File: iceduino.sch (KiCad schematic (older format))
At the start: 0 parts

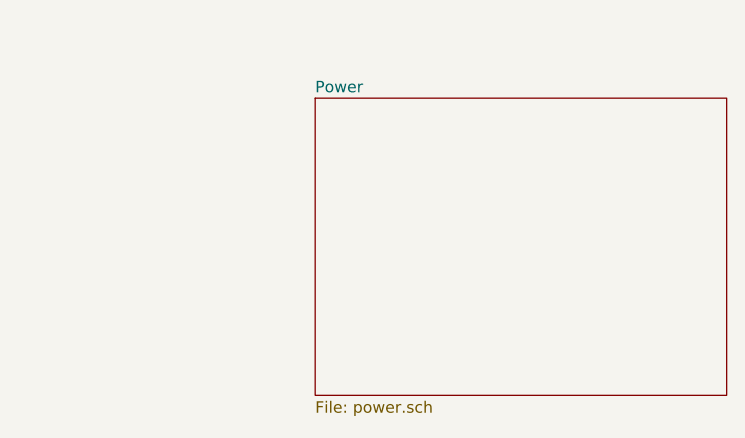
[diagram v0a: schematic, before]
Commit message: 7-17VIN Power
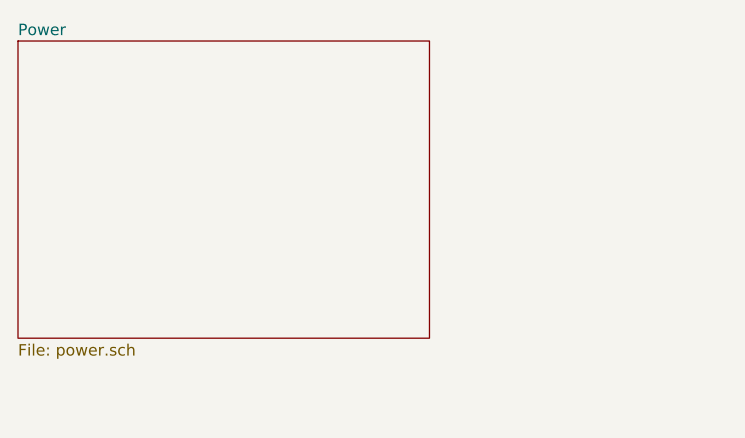
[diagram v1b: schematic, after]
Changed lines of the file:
@@
 $EndDescr
 $Sheet
-S 3250 2050 1800 1300
+S 1950 1800 1800 1300
 U 5ECD2614
 F0 "Power" 50

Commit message: ui sheet
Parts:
- added U?: ICE40HX4K-TQ144, symbol ice40hx4k:ICE40HX4K-TQ144
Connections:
- new net ADC_SCL_3V3: U?.120 (IOT_179)
- new net ADC_SDA_3V3: U?.121 (IOT_181)
- new net LED0: U?.112 (IOT_169)
- new net LED1: U?.113 (IOT_170)
- new net LED2: U?.114 (IOT_171)
- new net LED3: U?.115 (IOT_172)
- new net LED4: U?.116 (IOT_173)
- new net LED5: U?.117 (IOT_174)
- new net LED6: U?.118 (IOT_177)
- new net LED7: U?.119 (IOT_178)
- new net P10_1: U?.137 (IOT_215)
- new net P1_1: U?.143 (IOT_221)
- new net P2_1: U?.141 (IOT_219)
- new net P3_1: U?.138 (IOT_216)
- new net P4_1: U?.136 (IOT_214)
- new net P7_1: U?.144 (IOT_222)
- new net P8_1: U?.142 (IOT_220)
- new net P9_1: U?.139 (IOT_217)
- new net SW1: U?.122 (IOT_190)
- new net SW2: U?.124 (IOT_191)
- new net SW3: U?.125 (IOT_192)
- new net SW4: U?.128 (IOT_197_GBIN1)
- new net SW5: U?.129 (IOT_198_GBIN0)
- new net SW6: U?.130 (IOT_206)
- new net SW7: U?.134 (IOT_212)
- new net ~SRAM_CE~: U?.110 (IOT_168)
- no-connect marks 0 -> 1
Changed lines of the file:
@@
 $Descr A4 11693 8268
 encoding utf-8
-Sheet 1 6
+Sheet 1 7
 Title ""
 Date ""
@@
 F1 "power.sch" 50
 $EndSheet
+$Sheet
+S 5250 2350 1950 1200
+U 5F70B37B
+F0 "USER_INTERFACE" 50
+F1 "ui.sch" 50
+F2 "LED[0..7]" I L 5250 2950 50
+F3 "SW[1..7]" O R 7200 2950 50
+$EndSheet
+Wire Wire Line
+	8700 3000 8950 3000
+Text Label 8700 3000 0    50   ~ 0
+SW7
+Wire Wire Line
+	8700 2900 8950 2900
+Text Label 8700 2900 0    50   ~ 0
+SW6
+Wire Wire Line
+	8675 1300 8950 1300
+Text GLabel 8675 1300 0    39   Output ~ 0
+~SRAM_CE~
+Wire Wire Line
+	8700 2800 8950 2800
+Text Label 8700 2800 0    50   ~ 0
+SW5
+Wire Wire Line
+	8700 2700 8950 2700
+Text Label 8700 2700 0    50   ~ 0
+SW4
+Wire Wire Line
+	8700 2600 8950 2600
+Text Label 8700 2600 0    50   ~ 0
+SW3
+Wire Wire Line
+	8700 2500 8950 2500
+Text Label 8700 2500 0    50   ~ 0
+SW2
+Wire Wire Line
+	8700 2400 8950 2400
+Text Label 8700 2400 0    50   ~ 0
+SW1
+Wire Wire Line
+	8700 2100 8950 2100
+Text Label 8700 2100 0    50   ~ 0
+LED7
+Wire Wire Line
+	8700 2000 8950 2000
+Text Label 8700 2000 0    50   ~ 0
+LED6
+Wire Wire Line
+	8700 1900 8950 1900
+Text Label 8700 1900 0    50   ~ 0
+LED5
+Wire Wire Line
+	8700 1800 8950 1800
+Text Label 8700 1800 0    50   ~ 0
+LED4
+Wire Wire Line
+	8700 1700 8950 1700
+Text Label 8700 1700 0    50   ~ 0
+LED3
+Wire Wire Line
+	8700 1600 8950 1600
+Text Label 8700 1600 0    50   ~ 0
+LED2
+Wire Wire Line
+	8700 1500 8950 1500
+Text Label 8700 1500 0    50   ~ 0
+LED1
+Wire Wire Line
+	8700 1400 8950 1400
+Text Label 8700 1400 0    50   ~ 0
+LED0
+$Comp
+L ice40hx4k:ICE40HX4K-TQ144 U?
+U 2 1 5F791B82
+P 9150 2600
+AR Path="/5F791B82" Ref="U?"  Part="2"
+AR Path="/5CAB7CD4/5F791B82" Ref="U?"  Part="2"
+AR Path="/5F70B37B/5F791B82" Ref="U?"  Part="2"
+F 0 "U?" H 9150 1125 50  0000 L CNN
+F 1 "ICE40HX4K-TQ144" H 9350 4050 50  0000 L CNN
+F 2 "" H 9150 2600 50  0001 C CNN
+F 3 "" H 9150 2600 50  0001 C CNN
+F 4 "IC FPGA 107 I/O 144TQFP" H 700 -250 50  0001 C CNN "Description"
+F 5 "220-1572-ND" H 700 -250 50  0001 C CNN "Digikey"
+F 6 "Lattice Semiconductor Corporation" H 700 -250 50  0001 C CNN "Mfg Name"
+F 7 "ICE40HX4K-TQ144" H 700 -250 50  0001 C CNN "Mfg Part Num"
+F 8 "Spec" H 700 -250 50  0001 C CNN "Spec"
+	2    9150 2600
+	1    0    0    -1
+$EndComp
+NoConn ~ 8950 3100
+Wire Wire Line
+	8725 3900 8950 3900
+Wire Wire Line
+	8725 3700 8950 3700
+Wire Wire Line
+	8725 3500 8950 3500
+Wire Wire Line
+	8725 3300 8950 3300
+Wire Wire Line
+	8725 3800 8950 3800
+Wire Wire Line
+	8725 3600 8950 3600
+Wire Wire Line
+	8725 3400 8950 3400
+Wire Wire Line
+	8725 3200 8950 3200
+Text GLabel 8725 3800 0    50   BiDi ~ 0
+P1_1
+Text GLabel 8725 3600 0    50   BiDi ~ 0
+P2_1
+Text GLabel 8725 3400 0    50   BiDi ~ 0
+P3_1
+Text GLabel 8725 3200 0    50   BiDi ~ 0
+P4_1
+Text GLabel 8725 3900 0    50   BiDi ~ 0
+P7_1
+Text GLabel 8725 3700 0    50   BiDi ~ 0
+P8_1
+Text GLabel 8725 3500 0    50   BiDi ~ 0
+P9_1
+Text GLabel 8725 3300 0    50   BiDi ~ 0
+P10_1
+Text GLabel 8675 2300 0    50   BiDi ~ 0
+ADC_SDA_3V3
+Text GLabel 8675 2200 0    50   BiDi ~ 0
+ADC_SCL_3V3
+Wire Wire Line
+	8675 2200 8950 2200
+Wire Wire Line
+	8675 2300 8950 2300
+Wire Bus Line
+	7200 2950 7800 2950
+Wire Bus Line
+	5250 2950 4700 2950
+Text Label 4775 2950 0    50   ~ 0
+LED[0..7]
+Text Label 7400 2950 0    50   ~ 0
+SW[1..7]
 $EndSCHEMATC

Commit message: Schematic modified (Hierarchy) Bug where SPI was active when creset or ss was low fixed PCB layout started (almost all parts are at position) No parts on the bottom so far Arduino and PMOD header spacings corrected according to its standards
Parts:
- added D10, D9: CDBU5020, Diode_SMD:D_0603_1608Metric, symbol Device:D_ALT
- added H1, H2, H3, H4: MountingHole, MountingHole:MountingHole_3mm, symbol Mechanical:MountingHole
- added unit 1 of U1
- added unit 4 of U1
- added unit 5 of U1
- added unit 6 of U1
- added unit 7 of U1
- added unit 3 of U1
- U1: renamed from U?; footprint (none) -> Package_QFP:TQFP-144_20x20mm_P0.5mm
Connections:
- new net: D10.1 (K), U1.108 (VPP_2V5)
- new net: U1.133 (NC[7]), U1.35 (NC), U1.36 (NC), U1.50 (NC), U1.51 (NC), U1.58 (NC), U1.77 (NC)
- new net +1V2: U1.111 (VCC[4]), U1.27 (VCC), U1.40 (VCC), U1.92 (VCC)
- new net +3V3: D10.2 (A), U1.100 (VCCIO_1[2]), U1.123 (VCCIO_0), U1.131 (VCCIO_0[2]), U1.30 (VCCIO_3[2]), U1.46 (VCCIO_2), U1.57 (VCCIO_2[2]), U1.6 (VCCIO_3), U1.72 (VCC_SPI), U1.89 (VCCIO_1)
- new net A0: U1.73 (IOR_109)
- new net A1: U1.74 (IOR_110)
- new net A10: U1.101 (IOR_160)
- new net A11: U1.99 (IOR_152)
- new net A12: U1.98 (IOR_148)
- new net A13: U1.97 (IOR_147)
- new net A14: U1.96 (IOR_146)
- new net A15: U1.85 (IOR_128)
- new net A16: U1.83 (IOR_119)
- new net A17: U1.81 (IOR_117)
- new net A18: U1.79 (IOR_115)
- new net A2: U1.75 (IOR_111)
- new net A3: U1.76 (IOR_112)
- new net A4: U1.78 (IOR_114)
- new net A5: U1.102 (IOR_161)
- new net A6: U1.104 (IOR_164)
- new net A7: U1.105 (IOR_165)
- new net A8: U1.106 (IOR_166)
- new net A9: U1.107 (IOR_167)
- new net CDONE: U1.65 (CDONE)
- new net CLK_12M: U1.21 (IOL_14A_GBIN6)
- new net CRESET_B: D9.2 (A), U1.66 (CRESET_B)
- new net FPGA_INO_D2: U1.41 (IOB_63)
- new net FPGA_INO_D3: U1.42 (IOB_64)
- new net FPGA_INO_D4: U1.43 (IOB_71)
- new net FPGA_INO_D5: U1.44 (IOB_72)
- new net FPGA_INO_D6: U1.45 (IOB_73)
- new net FPGA_INO_D7: U1.47 (IOB_79)
- new net FPGA_INO_D8: U1.33 (IOL_25A)
- new net FPGA_INO_D9: U1.32 (IOL_24B)
- new net FPGA_INO_MISO: U1.25 (IOL_18A)
- new net FPGA_INO_MOSI: U1.29 (IOL_23B)
- new net FPGA_INO_RX: U1.38 (IOB_57)
- new net FPGA_INO_SCK: U1.24 (IOL_17B)
- new net FPGA_INO_SCL: U1.28 (IOL_23A)
- new net FPGA_INO_SDA: U1.26 (IOL_18B)
- new net FPGA_INO_SS: U1.31 (IOL_24A)
- new net FPGA_INO_TX: U1.37 (IOB_56)
- new net GND: U1.103 (GND), U1.13 (GND), U1.132 (GND), U1.14 (GND), U1.140 (GND[9]), U1.5 (GND), U1.59 (GND), U1.69 (GND), U1.86 (GND)
- new net GNDPLL_0: U1.53 (GNDPLL0)
- new net GNDPLL_1: U1.127 (GNDPLL1)
- new net IC_CLK_50M: U1.52 (IOB_82_GBIN4)
- new net INO_RESET: D9.1 (K)
- new net IO0: U1.80 (IOR_116)
- new net IO1: U1.82 (IOR_118)
- new net IO2: U1.84 (IOR_120)
- new net IO3: U1.91 (IOR_139)
- new net IO4: U1.95 (IOR_144)
- new net IO5: U1.93 (IOR_140_GBIN3)
- new net IO6: U1.90 (IOR_138)
- new net IO7: U1.88 (IOR_137)
- new net MISO: U1.68 (IOB_106_SDI)
- new net MOSI: U1.67 (IOB_105_SDO)
- new net OE0: U1.39 (IOB_61)
- new net OE1: U1.34 (IOL_25B)
- new net P10_2: U1.12 (IOL_8B)
- new net P10_3: U1.2 (IOL_2B)
- new net P1_2: U1.20 (IOL_13B_GBIN7)
- new net P1_3: U1.16 (IOL_10B)
- new net P2_2: U1.19 (IOL_13A)
- new net P2_3: U1.11 (IOL_8A)
- new net P3_2: U1.17 (IOL_12A)
- new net P3_3: U1.4 (IOL_3B)
- new net P4_2: U1.15 (IOL_10A)
- new net P4_3: U1.3 (IOL_3A)
- new net P7_2: U1.18 (IOL_12B)
- new net P7_3: U1.9 (IOL_5A)
- new net P8_2: U1.8 (IOL_4B)
- new net P8_3: U1.7 (IOL_4A)
- new net P9_2: U1.10 (IOL_5B)
- new net P9_3: U1.1 (IOL_2A)
- new net PMOD_PWR_EN: U1.22 (IOL_14B)
- new net RXD: U1.60 (IOB_95)
- new net SCK: U1.70 (IOB_107_SCK)
- new net SS: U1.71 (IOB_108_SS)
- new net TXD: U1.62 (IOB_102)
- new net VCCPLL_0: U1.54 (VCCPLL0)
- new net VCCPLL_1: U1.126 (VCCPLL1)
- new net ~CTS~: U1.56 (IOB_94)
- new net ~DCD~: U1.49 (IOB_81_GBIN5)
- new net ~DSR~: U1.55 (IOB_91)
- new net ~DTR~: U1.48 (IOB_80)
- new net ~RTS~: U1.61 (IOB_96)
- new net ~SRAM_OE~: U1.87 (IOR_136)
- new net ~SRAM_WE~: U1.94 (IOR_141_GBIN2)
- no-connect marks 1 -> 6
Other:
- note added: "Power for PLLs\nGND must not be connected\nto Board Ground"
- moved on the sheet: U1B

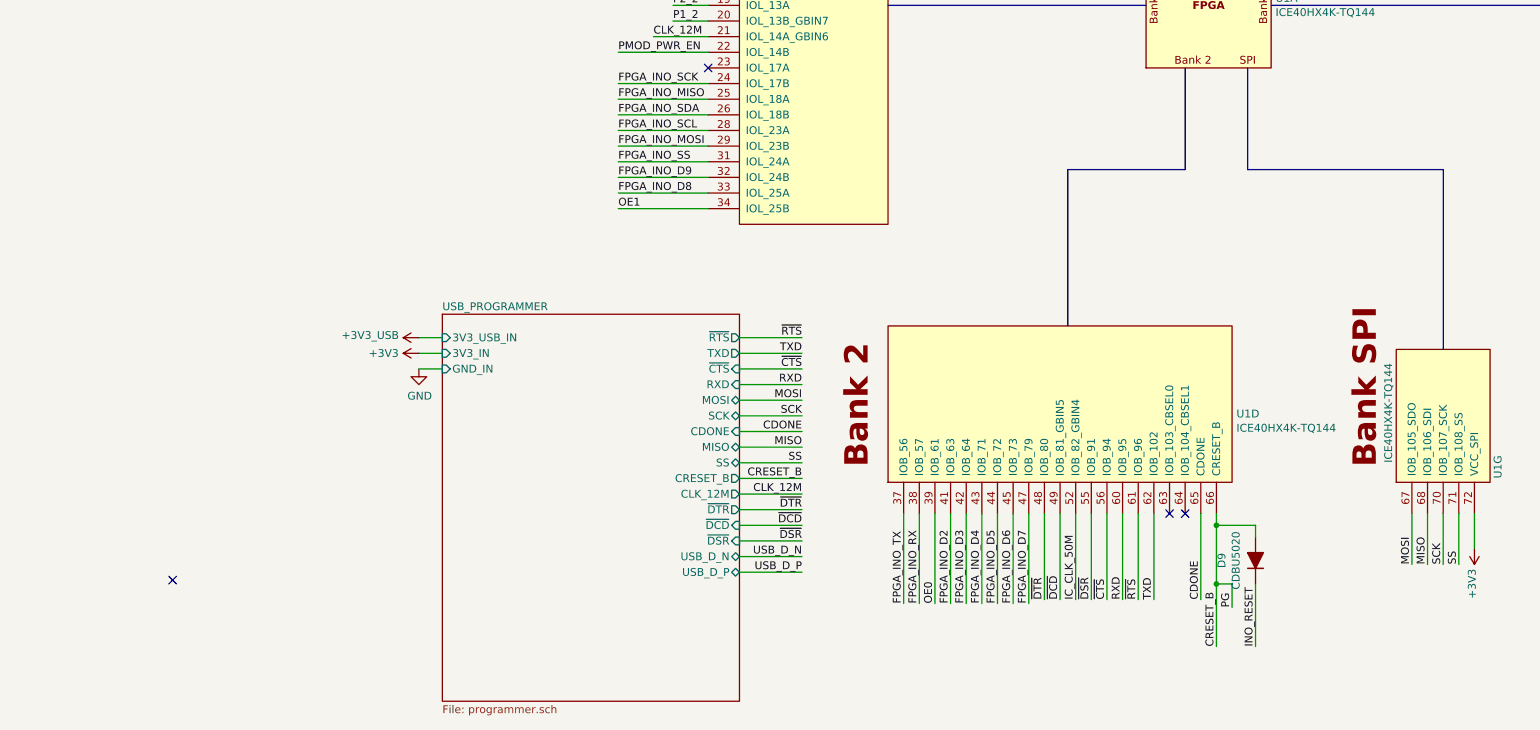
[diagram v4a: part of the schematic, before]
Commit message: Added wires for quad-SPI Flash operation
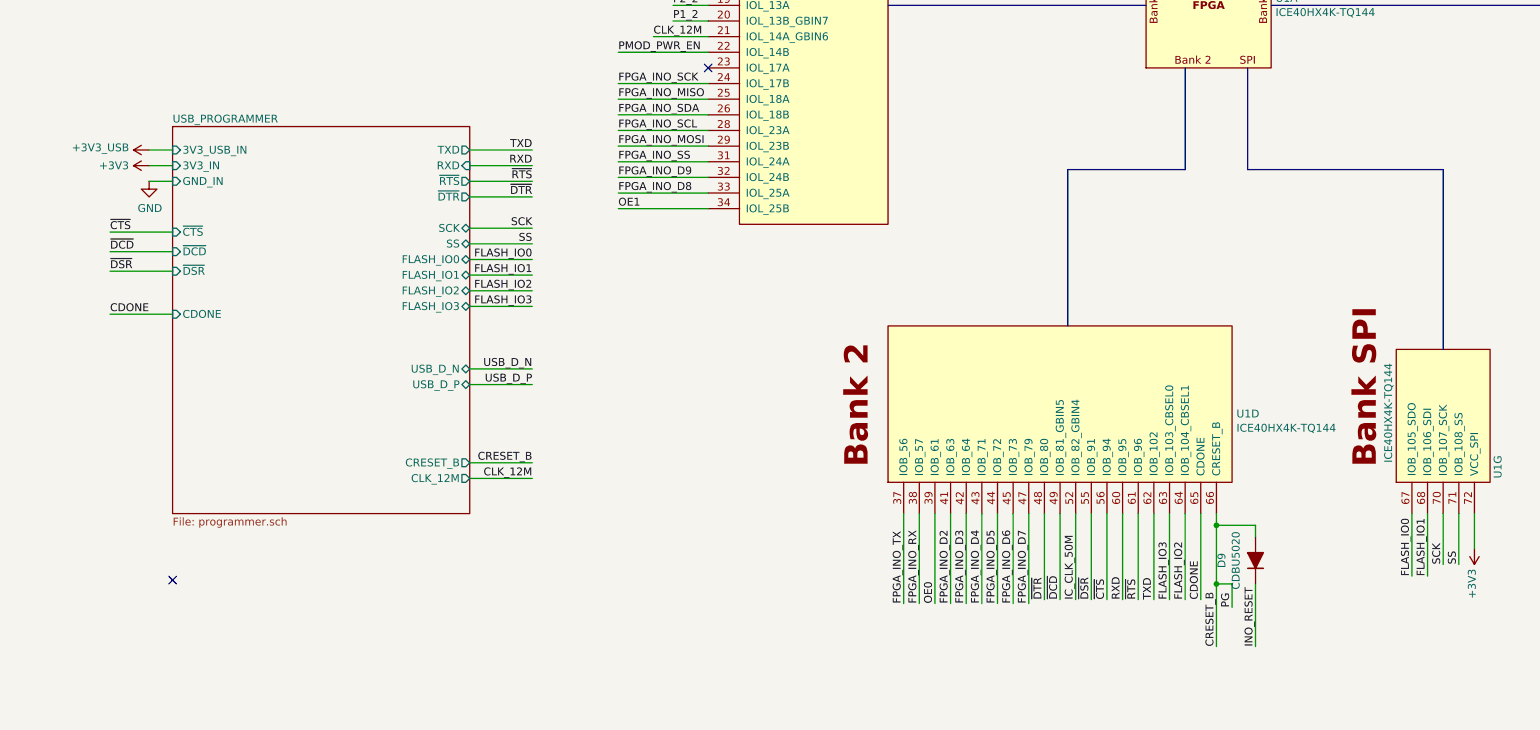
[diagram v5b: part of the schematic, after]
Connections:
- net FLASH_IO3: now reaches U1.63 (IOB_103_CBSEL0)
- net FLASH_IO2: now reaches U1.64 (IOB_104_CBSEL1)
- net MISO renamed FLASH_IO1
- net MOSI renamed FLASH_IO0
- no-connect marks 6 -> 4
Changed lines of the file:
@@
 Text Label 7350 9450 1    50   ~ 0
 IC_CLK_50M
-NoConn ~ 8050 8900
-NoConn ~ 7950 8900
 Wire Wire Line
 	8250 8900 8250 8975
@@
 	0    -1   -1   0
 $EndComp
-Text Label 9500 9225 1    50   ~ 0
-MOSI
-Wire Wire Line
-	9500 9225 9500 8900
-Text Label 9600 9225 1    50   ~ 0
-MISO
-Wire Wire Line
-	9600 9225 9600 8900
+Text Label 9500 9300 1    50   ~ 0
+FLASH_IO0
+Wire Wire Line
+	9500 9300 9500 8900
+Text Label 9600 9300 1    50   ~ 0
+FLASH_IO1
+Wire Wire Line
+	9600 9300 9600 8900
 Text Label 9700 9225 1    50   ~ 0
 SCK
@@
 Text Label 550  1250 0    50   ~ 0
 CDONE
-$Sheet
-S 3300 7625 1900 2475
-U 5ED0B946
-F0 "USB_PROGRAMMER" 50
-F1 "programmer.sch" 50
-F2 "3V3_USB_IN" I L 3300 7775 50
-F3 "3V3_IN" I L 3300 7875 50
-F4 "GND_IN" I L 3300 7975 50
-F5 "~RTS~" O R 5200 7775 50
-F6 "TXD" O R 5200 7875 50
-F7 "~CTS~" I R 5200 7975 50
-F8 "RXD" I R 5200 8075 50
-F9 "MOSI" B R 5200 8175 50
-F10 "SCK" B R 5200 8275 50
-F11 "CDONE" I R 5200 8375 50
-F12 "MISO" B R 5200 8475 50
-F13 "SS" B R 5200 8575 50
-F14 "CRESET_B" O R 5200 8675 50
-F15 "CLK_12M" O R 5200 8775 50
-F16 "~DTR~" O R 5200 8875 50
-F17 "~DCD~" I R 5200 8975 50
-F18 "~DSR~" I R 5200 9075 50
-F19 "USB_D_N" B R 5200 9175 50
-F20 "USB_D_P" B R 5200 9275 50
-$EndSheet
-Wire Wire Line
-	3300 7775 3150 7775
-Wire Wire Line
-	3300 7875 3150 7875
-Wire Wire Line
-	3300 7975 3150 7975
+Wire Wire Line
+	1575 6575 1425 6575
+Wire Wire Line
+	1575 6675 1425 6675
+Wire Wire Line
+	1575 6775 1425 6775
 $Comp
 L power_symbols:+3V3_USB #PWR01
 U 1 1 5F14A03A
-P 3150 7775
-F 0 "#PWR01" H 3150 7625 50  0001 C CNN
-F 1 "+3V3_USB" V 3165 7903 50  0000 L CNN
-F 2 "" H 3150 7775 50  0001 C CNN
-F 3 "" H 3150 7775 50  0001 C CNN
-	1    3150 7775
+P 1425 6575
+F 0 "#PWR01" H 1425 6425 50  0001 C CNN
+F 1 "+3V3_USB" V 1440 6703 50  0000 L CNN
+F 2 "" H 1425 6575 50  0001 C CNN
+F 3 "" H 1425 6575 50  0001 C CNN
+	1    1425 6575
 	0    -1   -1   0
 $EndComp
@@
 L power:GND #PWR03
 U 1 1 5F18E191
-P 3150 7975
-F 0 "#PWR03" H 3150 7725 50  0001 C CNN
-F 1 "GND" H 3155 7802 50  0000 C CNN
-F 2 "" H 3150 7975 50  0001 C CNN
-F 3 "" H 3150 7975 50  0001 C CNN
-	1    3150 7975
-	1    0    0    -1
-$EndComp
-Wire Wire Line
-	5200 7775 5600 7775
-Wire Wire Line
-	5200 7875 5600 7875
-Wire Wire Line
-	5200 7975 5600 7975
-Wire Wire Line
-	5200 8075 5600 8075
-Wire Wire Line
-	5200 8175 5600 8175
-Wire Wire Line
-	5200 8275 5600 8275
-Wire Wire Line
-	5200 8375 5600 8375
-Wire Wire Line
-	5200 8475 5600 8475
-Wire Wire Line
-	5200 8575 5600 8575
-Wire Wire Line
-	5200 8675 5600 8675
-Wire Wire Line
-	5200 8775 5600 8775
-Wire Wire Line
-	5200 8875 5600 8875
-Wire Wire Line
-	5200 8975 5600 8975
-Wire Wire Line
-	5200 9075 5600 9075
-Text Label 5600 7775 2    50   ~ 0
+P 1425 6775
+F 0 "#PWR03" H 1425 6525 50  0001 C CNN
+F 1 "GND" H 1430 6602 50  0000 C CNN
+F 2 "" H 1425 6775 50  0001 C CNN
+F 3 "" H 1425 6775 50  0001 C CNN
+	1    1425 6775
+	1    0    0    -1
+$EndComp
+Wire Wire Line
+	3475 6775 3875 6775
+Wire Wire Line
+	3475 6575 3875 6575
+Wire Wire Line
+	1575 7100 1175 7100
+Wire Wire Line
+	3475 6675 3875 6675
+Wire Wire Line
+	3475 7275 3875 7275
+Wire Wire Line
+	3475 7075 3875 7075
+Wire Wire Line
+	1575 7625 1175 7625
+Wire Wire Line
+	3475 7375 3875 7375
+Wire Wire Line
+	3475 7175 3875 7175
+Wire Wire Line
+	3475 8575 3875 8575
+Wire Wire Line
+	3475 8675 3875 8675
+Wire Wire Line
+	3475 6875 3875 6875
+Wire Wire Line
+	1575 7225 1175 7225
+Wire Wire Line
+	1575 7350 1175 7350
+Text Label 3875 6775 2    50   ~ 0
 ~RTS~
-Text Label 5600 7875 2    50   ~ 0
+Text Label 3875 6575 2    50   ~ 0
 TXD
-Text Label 5600 7975 2    50   ~ 0
+Text Label 1175 7100 0    50   ~ 0
 ~CTS~
-Text Label 5600 8075 2    50   ~ 0
+Text Label 3875 6675 2    50   ~ 0
 RXD
-Text Label 5600 8175 2    50   ~ 0
-MOSI
-Text Label 5600 8275 2    50   ~ 0
+Text Label 3875 7275 2    50   ~ 0
+FLASH_IO0
+Text Label 3875 7075 2    50   ~ 0
 SCK
-Text Label 5600 8375 2    50   ~ 0
+Text Label 1175 7625 0    50   ~ 0
 CDONE
-Text Label 5600 8475 2    50   ~ 0
-MISO
-Text Label 5600 8575 2    50   ~ 0
+Text Label 3875 7375 2    50   ~ 0
+FLASH_IO1
+Text Label 3875 7175 2    50   ~ 0
 SS
-Text Label 5600 8675 2    50   ~ 0
+Text Label 3875 8575 2    50   ~ 0
 CRESET_B
-Text Label 5600 8775 2    50   ~ 0
+Text Label 3875 8675 2    50   ~ 0
 CLK_12M
-Text Label 5600 8875 2    50   ~ 0
+Text Label 3875 6875 2    50   ~ 0
 ~DTR~
-Text Label 5600 8975 2    50   ~ 0
+Text Label 1175 7225 0    50   ~ 0
 ~DCD~
-Text Label 5600 9075 2    50   ~ 0
+Text Label 1175 7350 0    50   ~ 0
 ~DSR~
 Text Label 7150 9450 1    50   ~ 0
@@
 	4650 5850 5000 5850
 Wire Wire Line
-	5200 9175 5600 9175
-Wire Wire Line
-	5200 9275 5600 9275
-Text Label 5600 9175 2    50   ~ 0
+	3475 7975 3875 7975
+Wire Wire Line
+	3475 8075 3875 8075
+Text Label 3875 7975 2    50   ~ 0
 USB_D_N
-Text Label 5600 9275 2    50   ~ 0
+Text Label 3875 8075 2    50   ~ 0
 USB_D_P
 $Comp
@@
 L power:+3V3 #PWR0107
 U 1 1 5F527E84
-P 3150 7875
-F 0 "#PWR0107" H 3150 7725 50  0001 C CNN
-F 1 "+3V3" V 3150 8100 50  0000 C CNN
-F 2 "" H 3150 7875 50  0001 C CNN
-F 3 "" H 3150 7875 50  0001 C CNN
-	1    3150 7875
+P 1425 6675
+F 0 "#PWR0107" H 1425 6525 50  0001 C CNN
+F 1 "+3V3" V 1425 6900 50  0000 C CNN
+F 2 "" H 1425 6675 50  0001 C CNN
+F 3 "" H 1425 6675 50  0001 C CNN
+	1    1425 6675
 	0    -1   -1   0
 $EndComp
@@
 	1    0    0    -1
 $EndComp
+Wire Wire Line
+	3475 7475 3875 7475
+Wire Wire Line
+	3475 7575 3875 7575
+Text Label 3875 7475 2    50   ~ 0
+FLASH_IO2
+Wire Wire Line
+	7950 8900 7950 9450
+Wire Wire Line
+	8050 8900 8050 9450
+Text Label 8050 9450 1    50   ~ 0
+FLASH_IO2
+$Sheet
+S 1575 6425 1900 2475
+U 5ED0B946
+F0 "USB_PROGRAMMER" 50
+F1 "programmer.sch" 50
+F2 "3V3_USB_IN" I L 1575 6575 50
+F3 "3V3_IN" I L 1575 6675 50
+F4 "GND_IN" I L 1575 6775 50
+F5 "~RTS~" O R 3475 6775 50
+F6 "TXD" O R 3475 6575 50
+F7 "~CTS~" I L 1575 7100 50
+F8 "RXD" I R 3475 6675 50
+F9 "FLASH_IO0" B R 3475 7275 50
+F10 "SCK" B R 3475 7075 50
+F11 "CDONE" I L 1575 7625 50
+F12 "FLASH_IO1" B R 3475 7375 50
+F13 "SS" B R 3475 7175 50
+F14 "CRESET_B" O R 3475 8575 50
+F15 "CLK_12M" O R 3475 8675 50
+F16 "~DTR~" O R 3475 6875 50
+F17 "~DCD~" I L 1575 7225 50
+F18 "~DSR~" I L 1575 7350 50
+F19 "USB_D_N" B R 3475 7975 50
+F20 "USB_D_P" B R 3475 8075 50
+F21 "FLASH_IO2" B R 3475 7475 50
+F22 "FLASH_IO3" B R 3475 7575 50
+$EndSheet
+Text Label 3875 7575 2    50   ~ 0
+FLASH_IO3
+Text Label 7950 9450 1    50   ~ 0
+FLASH_IO3
 $EndSCHEMATC
